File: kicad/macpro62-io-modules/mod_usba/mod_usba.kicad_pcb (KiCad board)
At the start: 2 copper layers, 39.7 x 8.8 mm, 5 parts, among them J1 MOD-A - kinghelm KH-3.0AF180Z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, J2 DF40C-50DP-0.4V(51) C424645 -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, U1 24C02 WLCSP-4 ID EEPROM @0x50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

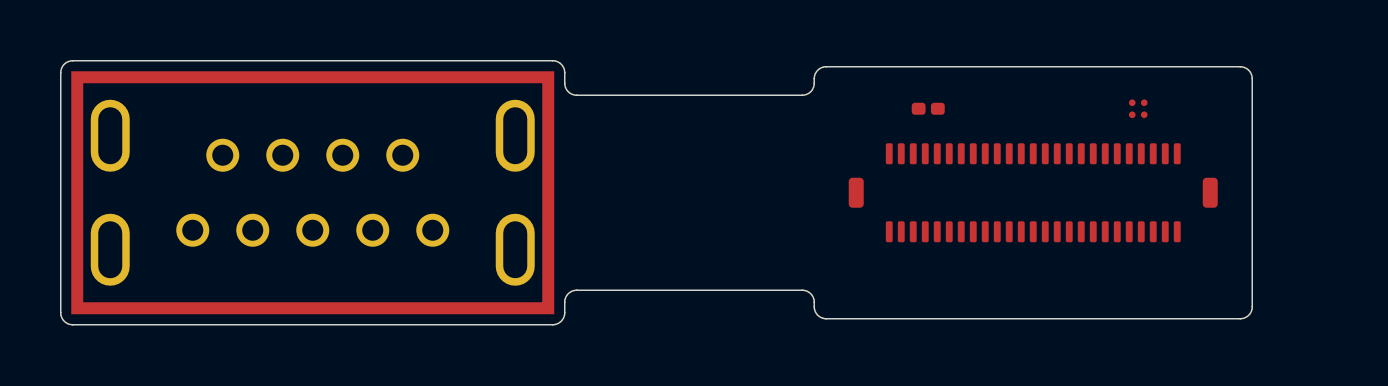
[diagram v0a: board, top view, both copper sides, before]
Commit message: I/O plate: centre + corner M1.6 frame screws, screwpt variant, plate fixes, module routing, ESD
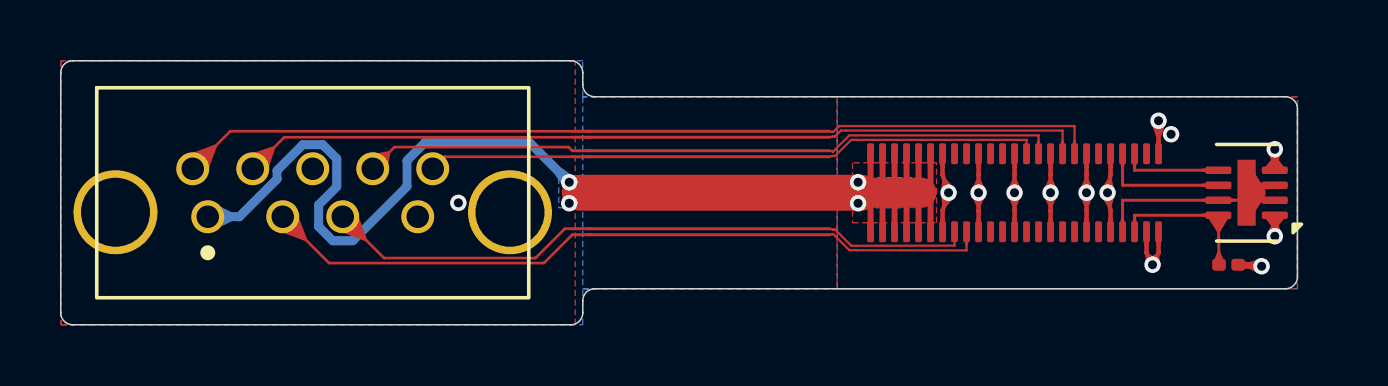
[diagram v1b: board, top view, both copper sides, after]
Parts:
- removed G1: sleeve GND ring (SUS304 0.2 sleeve, bonded to the shell), MP62_MOD:MP62_MOD_Sleeve_GND_Ring_USBA
- C1: value 100nF 0201 (3V3_MOD) -> 100nF 0201 X5R 10V (3V3_MOD)
- J1: value MOD-A - kinghelm KH-3.0AF180ZJ-11.5JB (C2979037) THT -> MOD-A - Hong Cheng HC-USB3.0-L137-WJ (C7501870) THT, H 13.7; alt kinghelm KH-3.0AF180ZJ-11.5JB (C2979037, H 11.5); footprint MP62_MOD:MP62_USB_A3_9P_Vertical_PLACEHOLDER -> MP62_MOD:MP62_MOD_USB_A3_HC-USB3.0-L137-WJ
- J2: value DF40C-50DP-0.4V(51) C424645 -> main-board JMn DF40C-50DS (PMI-50 pinout) -> DF40C-50DP-0.4V(51) C424645 -> JMn DF40C-50DS (PMI-50 v2)
- U1: value 24C02 WLCSP-4 ID EEPROM @0x50 (MOD ID / type / rev / serial) -> BL24C02F-NTRC (C2828222) 24C02 ID EEPROM @0x50; footprint MP62_MOD:MP62_WLCSP-4_0.8x0.8_P0.4_EEPROM -> MP62_MOD:DFN-8-1EP_2x3mm_P0.5mm_EP0.61x2.2mm
- moved C1 11.3 mm to (130.5, 102.4)
- moved U1 4.57 mm to (131.1, 100.0), turned to 180 degrees
- moved J2 0.62 mm to (123.4, 100.0)
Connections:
- C1 pad 1: (no net) -> 3V3_MOD
- C1 pad 2: (no net) -> GND
- J1 pad 1: (no net) -> VBUS
- J1 pad 2: (no net) -> D_N
- J1 pad 3: (no net) -> D_P
- J1 pad 4: (no net) -> GND
- J1 pad 5: (no net) -> SSRX_N
- J1 pad 6: (no net) -> SSRX_P
- J1 pad 7: (no net) -> GND
- J1 pad 8: (no net) -> SSTX_N
- J1 pad 9: (no net) -> SSTX_P
- J1 pad S: (no net) -> GND
- J2 pad 1: (no net) -> VBUS
- J2 pad 10: (no net) -> VBUS
- J2 pad 11: (no net) -> VBUS
- J2 pad 12: (no net) -> VBUS
- J2 pad 13: (no net) -> GND
- J2 pad 14: (no net) -> GND
- J2 pad 16: (no net) -> D_P
- J2 pad 18: (no net) -> D_N
- J2 pad 19: (no net) -> GND
- J2 pad 2: (no net) -> VBUS
- J2 pad 20: (no net) -> GND
- J2 pad 25: (no net) -> GND
- J2 pad 26: (no net) -> GND
- J2 pad 27: (no net) -> SSRX_N
- J2 pad 29: (no net) -> SSRX_P
- J2 pad 3: (no net) -> VBUS
- J2 pad 31: (no net) -> GND
- J2 pad 32: (no net) -> GND
- J2 pad 33: (no net) -> SSTX_N
- J2 pad 35: (no net) -> SSTX_P
- J2 pad 37: (no net) -> GND
- J2 pad 38: (no net) -> GND
- J2 pad 4: (no net) -> VBUS
- J2 pad 41: (no net) -> GND
- J2 pad 42: (no net) -> GND
- J2 pad 43: (no net) -> ID_SCL
- J2 pad 44: (no net) -> GND
- J2 pad 45: (no net) -> ID_SDA
- J2 pad 46: (no net) -> 3V3_MOD
- J2 pad 48: (no net) -> GND
- J2 pad 49: (no net) -> GND
- J2 pad 5: (no net) -> VBUS
- J2 pad 50: (no net) -> GND
- J2 pad 6: (no net) -> VBUS
- J2 pad 7: (no net) -> VBUS
- J2 pad 8: (no net) -> VBUS
- J2 pad 9: (no net) -> VBUS
- U1 pad 1: (no net) -> GND
- U1 pad 2: (no net) -> GND
- U1 pad 3: (no net) -> GND
- U1 pad 4: (no net) -> GND
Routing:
- net VBUS: track 0.00 -> 47.1 mm, vias 0 -> 4
- net SSTX_P: track 0.00 -> 30.9 mm
- net GND: track 0.00 -> 28.3 mm, vias 0 -> 13
- net SSTX_N: track 0.00 -> 28.3 mm
- net D_N: track 0.00 -> 24.7 mm
- net SSRX_P: track 0.00 -> 23.4 mm
- net D_P: track 0.00 -> 22.1 mm
- net SSRX_N: track 0.00 -> 20.6 mm
- net 3V3_MOD: track 0.00 -> 5.00 mm
- net ID_SCL: track 0.00 -> 4.24 mm
- net ID_SDA: track 0.00 -> 3.34 mm
- added copper zone on B.Cu, net GND
- added copper zone on F.Cu, net GND
- added copper zone on B.Cu, net VBUS
- added copper zone on F.Cu, net VBUS
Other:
- board size 39.7 x 8.8 mm -> 41.2 x 8.8 mm
- board text added: "FR4 0.6 stiffener (B) under the header paddle"
- board text added: "FR4 1.0 stiffener (B, PSA) under the port"
- board text added: "cradle ledges (stiffener bottom bears here, 1.0 wide)"
- board text added: "loop-fold 180 deg, R 1.65-1.66 = 15-15 x t (bend zone: no vias / parts, hatched L2)"
- board text removed: "C-fold 180 deg, R 2.33 (bend zone: no vias, no parts, staggered traces)"
- board text removed: "FR4 1.0 stiffener (B) under the header paddle"
- board text removed: "FR4 1.0 stiffener (B, flush, PSA) under the port"
- board text removed: "Fits slots A1, A2, A3, A4. Electrical length port pads -> header ~26 mm."
- board text removed: "MOD-A, unfolded. Port at (0,0); u -> outboard edge. Stiffener 16.8 x 8.8; tail 6.5 wide; flap 0.5; fold R 2.33; paddle 14.6 x 8.4."
- board text removed: "PMI-50 (J2 odd/even): 13/14 GND/GND; 15/16 GND/GND; 17/18 HS0_P/HS2_P; 19/20 HS0_N/HS2_N; 21/22 GND/GND; 23/24 HS1_P/HS3_P; 25/26 HS1_N/HS3_N; 27/28 GND/GND; 29/30 USB2_DP/SBU1; 31/32 USB2_DN/SBU2; 33/34 GND/GND; 35/36 CC1/HPD; 37/38 CC2/UTIL; 39/40 GND/GND; 41/42 ID_SCL/ID_SDA; 43/44 3V3_MOD/PRSNT#; 45/46 LED#/GND; 47/48 GND/GND; 49/50 GND/GND"
- board text removed: "Plug loads: push -> connector body -> FPC -> FR4 stiffener -> cradle ledges; pull/side -> bonded SUS sleeve -> collar -> clamp plate -> screws. Not through solder or flex."
- board text removed: "cradle ledges (stiffener bottom bears here; no parts / THT tips in the bands)"
- board text removed: "optional silver EMI film (F), >= 0.8 from stiffeners, GND openings D1.0 at both ends"

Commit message: USB-C flex module routed (HYCW417, 0 DRC, matched pairs), 3-mil min on flexes, two flex panels, CH334F + ASM1182e QFN-48 footprints
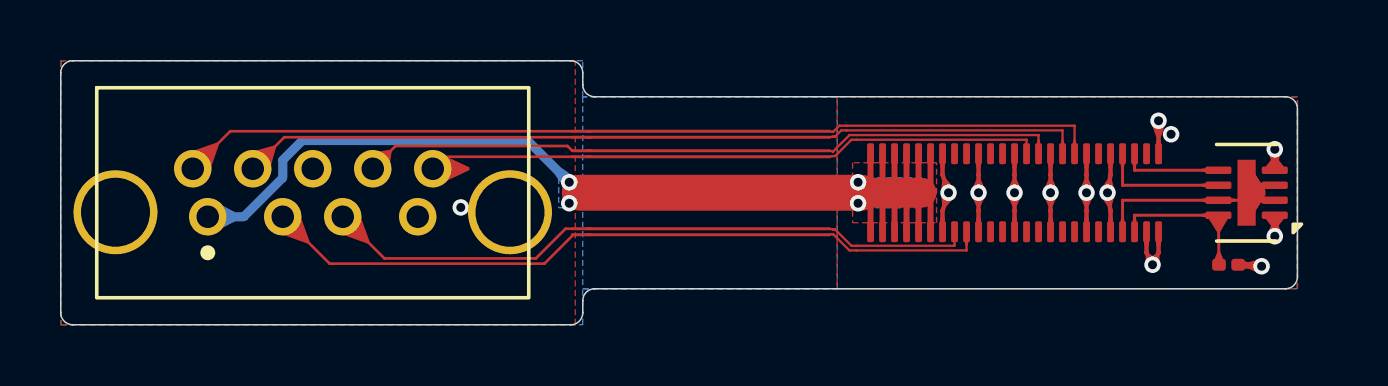
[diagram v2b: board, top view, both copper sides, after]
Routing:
- net VBUS: track 47.1 -> 42.0 mm

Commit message: Plate test-print fixes (corners +1mm Y, C2 post -1mm, C1 removed); USB-A/HDMI hand fan-out 0 skew; real DF40 + HDMI footprints
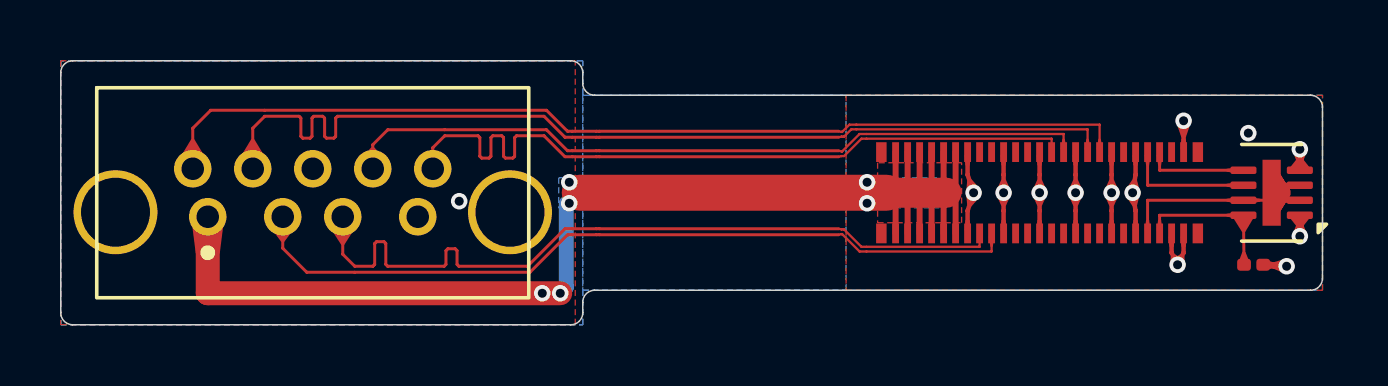
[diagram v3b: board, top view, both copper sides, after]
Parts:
- J2: footprint MP62_MOD:MP62_Hirose_DF40C-50DP-0.4V_PLACEHOLDER -> MP62_MOD:MP62_Hirose_DF40C-50DP-0.4V
- moved C1 0.84 mm to (131.4, 102.4)
- moved U1 0.84 mm to (132.0, 100.0)
- moved J2 0.83 mm to (124.2, 100.0)
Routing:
- net SSTX_N: track 28.3 -> 33.1 mm
- net VBUS: track 42.0 -> 46.8 mm, vias 4 -> 6
- net SSRX_N: track 20.7 -> 25.2 mm
- net D_P: track 22.1 -> 26.4 mm
- net SSTX_P: track 30.9 -> 33.1 mm
- net SSRX_P: track 23.4 -> 25.2 mm
- net D_N: track 24.7 -> 26.4 mm
- net GND: track 28.3 -> 28.9 mm
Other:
- board size 41.2 x 8.8 mm -> 42.1 x 8.8 mm
